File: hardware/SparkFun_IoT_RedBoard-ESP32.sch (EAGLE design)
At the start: 115 parts, among them J1 5.5x2.1mm Barrel, J13 QWIIC_RIGHT_ANGLE, J15 MICRO-SD-PUSH-PUSH-EXT-PIN, J2 USB C, J3 USB_SOLDER_PADS, J5 M10NO_SILK, Q1 MBT3904DW1T1, Q11 20V/4.2A/52mΩ/1.4W, Q13 20V/4.2A/52mΩ/1.4W, Q3 20V/4.2A/52mΩ/1.4W, Q5 20V/4.2A/52mΩ/1.4W, Q7 20V/4.2A/52mΩ/1.4W, Q9 20V/4.2A/52mΩ/1.4W, U1 ESP-WROOM-3232D-NARROW, U2 CH340C, U3 LM1117, U4 3.3V, U5 MCP73831, U6 MAX17048

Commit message: Design review updates
Rename files to remove "v01"
Update libraries
Adjust traces under SD card for keepout region
Change ESP32 footprint from narrow to standard
Change USB-C connector to 4-layer version
Add USB shield jumper
Move CC resistor positions
Adjust parts to be on grid where possible
Move Qwiic logo to top silk (also adjust Reset silk to avoid confusion)
Adjust layer numbers in copper to not overlap
Remove C14
Increase current rating of D1
Add silk to addressable LED
Remove extraneous mill lines
Remove Made in USA silk
Replace MEAS header and jumper with combo jumper
Add fuse value to schematic
Remove voltage ratings from capacitors in schematic
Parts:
- removed C14: 10uF, SparkFun-Capacitors:10UF-0603-6.3V-20%
- removed J14: (no value), SparkFun-Connectors:CONN_021X02_NO_SILK
- added JP15: SHLD, SparkFun-Jumpers:JUMPER-SMT_2_NC_TRACE_SILK
- D1: value 1A/40V/500mV -> 3A/40V/500mV; device SparkFun-DiscreteSemi:DIODE-SCHOTTKY-SS14 -> SparkFun-DiscreteSemi:DIODE-SCHOTTKY-B340A
- F1: value 6V/0.75A -> 6V/0.75A/1.5A
- J2: value USB C -> USB-C; device SparkFun-Connectors:USB_C_2-LAYER_PADS -> SparkFun-Connectors:USB_C_4-LAYER-ISOLATED
- JP10: value JUMPER-SMT_2_NC_TRACE_SILK -> JUMPER-COMBO_2_NC_TRACE; device SparkFun-Jumpers:JUMPER-SMT_2_NC_TRACE_SILK -> SparkFun-Jumpers:JUMPER-COMBO_2_NC_TRACE
- U1: value ESP-WROOM-3232D-NARROW -> ESP-WROOM-3232D; device SparkFun-RF:ESP-WROOM-3232D-NARROW -> SparkFun-RF:ESP-WROOM-3232D
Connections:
- new net SHLD: J2.SHLD, JP15.2
- net !DTR!: now also Q1G1.E; no longer Q1Q1.E
- net !RTS!: now also Q1G2.E; no longer Q1Q2.E
- net 3.3V: no longer C14.1
- net 5V_CHG: now also Q10G2.E, Q12G2.E; no longer Q10G$2.E, Q12G$2.E
- net 5V_EXT: now also Q12G1.E, Q6G1.E; no longer Q12G$1.E, Q6G$1.E
- net 5V_MEAS: now also Q4G2.E, Q6G2.E, Q8G2.E; no longer J14.2, Q4G$2.E, Q6G$2.E, Q8G$2.E
- net ESP32_0: now also Q1G1.C; no longer Q1Q1.C
- net ESP32_EN: now also Q1G2.C; no longer Q1Q2.C
- net GND: now also JP15.1, Q2G1.E, Q2G2.E; no longer C14.2, Q2Q1.E, Q2Q2.E
- net N$10: now also Q6G2.C; no longer Q6G$2.C
- net N$11: now also Q2G1.C; no longer Q2Q1.C
- net N$12: now also Q4G1.B, Q4G1.C, Q4G2.B; no longer Q4G$1.B, Q4G$1.C, Q4G$2.B
- net N$13: now also Q8G1.B, Q8G1.C, Q8G2.B; no longer Q8G$1.B, Q8G$1.C, Q8G$2.B
- net N$16: now also Q4G2.C; no longer Q4G$2.C
- net N$17: now also Q8G2.C; no longer Q8G$2.C
- net N$19: no longer J14.1
- net N$21: now also Q2G2.B; no longer Q2Q2.B
- net N$22: now also Q2G1.B, Q2G2.C; no longer Q2Q1.B, Q2Q2.C
- net N$23: now also Q10G2.C; no longer Q10G$2.C
- net N$24: now also Q1G1.B; no longer Q1Q1.B
- net N$25: now also Q1G2.B; no longer Q1Q2.B
- net N$26: now also Q10G1.B, Q10G1.C, Q10G2.B; no longer Q10G$1.B, Q10G$1.C, Q10G$2.B
- net N$28: now also Q12G2.C; no longer Q12G$2.C
- net N$29: now also Q12G1.B, Q12G1.C, Q12G2.B; no longer Q12G$1.B, Q12G$1.C, Q12G$2.B
- net N$8: now also Q6G1.B, Q6G1.C, Q6G2.B; no longer Q6G$1.B, Q6G$1.C, Q6G$2.B
- net VUSB_PROT: now also Q4G1.E; no longer Q4G$1.E
- net V_BATT: now also Q8G1.E; no longer Q8G$1.E
- net V_USB: now also Q10G1.E; no longer Q10G$1.E
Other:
- note added: "Open jumper to measure board current on J10"
- note removed: "16V"
- note removed: "25V"
- note removed: "35V"
- note removed: "Open jumper to measure board current on J14"
- moved on the sheet: C12, C13, J2, J3, U4

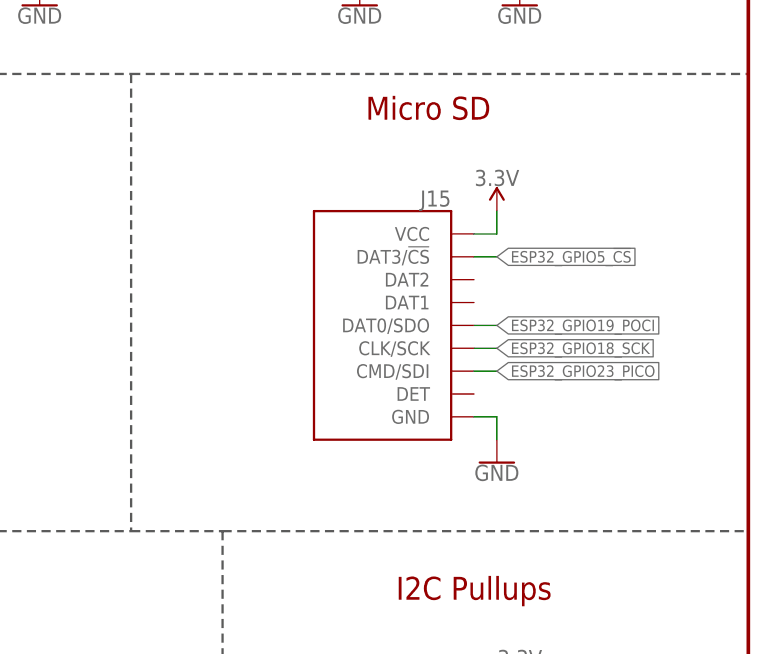
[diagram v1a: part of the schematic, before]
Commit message: More design review updates
Add center positive silk marker to barrel jack
Fix air wire errors in ULP by connecting with traces
Add SD card detection with NO jumper to GPIO16
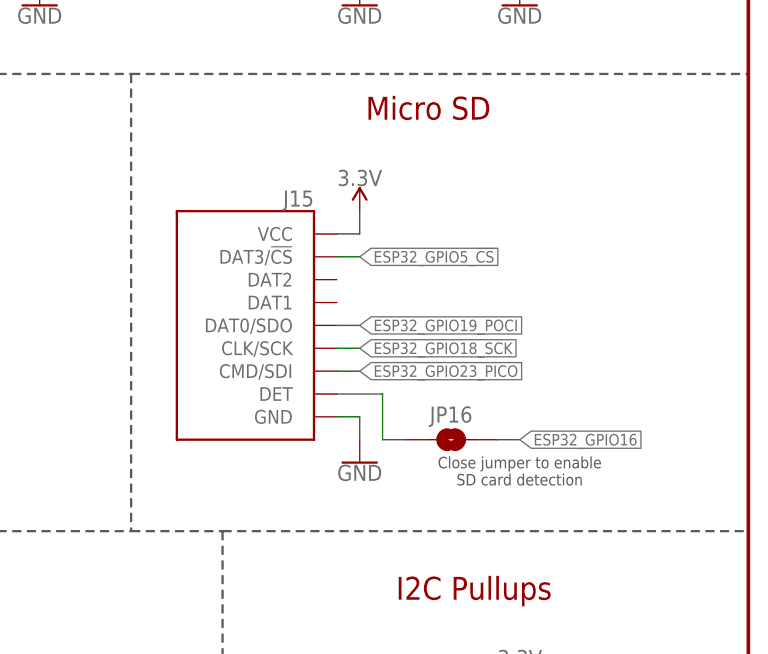
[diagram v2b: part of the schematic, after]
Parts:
- added JP16: SD_DET, SparkFun-Jumpers:JUMPER-SMT_2_NO_SILK
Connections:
- new net N$27: J15.DET, JP16.1
- net ESP32_GPIO16: now also JP16.2
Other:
- note added: "Close jumper to enable SD card detection"
- moved on the sheet: J15
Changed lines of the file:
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@@
 <part name="GND56" library="SparkFun-PowerSymbols" deviceset="GND" device=""/>
 <part name="F1" library="SparkFun-Fuses" deviceset="PPTC" device="_0.75A" value="6V/0.75A/1.5A"/>
+<part name="JP16" library="SparkFun-Jumpers" deviceset="JUMPER-SMT_2_NO" device="_SILK" package3d_urn="urn:adsk.eagle:package:39279/1" value="SD_DET"/>
 </parts>
 <sheets>
@@
 <wire x1="317.5" y1="203.2" x2="317.5" y2="236.22" width="0.254" layer="97" style="longdash"/>
 <text x="330.2" y="228.6" size="2.54" layer="94" font="vector" ratio="11" align="bottom-center">RGB LED</text>
+<text x="406.4" y="93.98" size="1.27" layer="97" font="vector" align="bottom-center">Close jumper to enable
+SD card detection</text>
 </plain>
 <instances>
@@
 <attribute name="VALUE" x="50.8" y="152.908" size="1.778" layer="96" font="vector" rot="R180" align="center" display="off"/>
 </instance>
-<instance part="J15" gate="J1" x="393.7" y="111.76" smashed="yes" rot="MR0">
-<attribute name="NAME" x="398.78" y="124.968" size="1.778" layer="95" rot="MR0"/>
-<attribute name="VALUE" x="398.78" y="96.52" size="1.778" layer="96" rot="MR0" display="off"/>
-</instance>
-<instance part="SUPPLY27" gate="G$1" x="403.86" y="124.46" smashed="yes">
-<attribute name="VALUE" x="403.86" y="127.254" size="1.778" layer="96" align="bottom-center"/>
-</instance>
-<instance part="GND33" gate="1" x="403.86" y="96.52" smashed="yes">
-<attribute name="VALUE" x="403.86" y="96.266" size="1.778" layer="96" align="top-center"/>
+<instance part="J15" gate="J1" x="378.46" y="111.76" smashed="yes" rot="MR0">
+<attribute name="NAME" x="383.54" y="124.968" size="1.778" layer="95" rot="MR0"/>
+<attribute name="VALUE" x="383.54" y="96.52" size="1.778" layer="96" rot="MR0" display="off"/>
+</instance>
+<instance part="SUPPLY27" gate="G$1" x="388.62" y="124.46" smashed="yes">
+<attribute name="VALUE" x="388.62" y="127.254" size="1.778" layer="96" align="bottom-center"/>
+</instance>
+<instance part="GND33" gate="1" x="388.62" y="96.52" smashed="yes">
+<attribute name="VALUE" x="388.62" y="96.266" size="1.778" layer="96" align="top-center"/>
 </instance>
 <instance part="GND24" gate="1" x="144.78" y="5.08" smashed="yes">
@@
 <attribute name="NAME" x="159.893" y="15.113" size="1.778" layer="95" font="vector" align="bottom-center"/>
 <attribute name="VALUE" x="161.29" y="9.906" size="1.778" layer="96" font="vector" align="top-center"/>
+</instance>
+<instance part="JP16" gate="G$1" x="398.78" y="99.06" smashed="yes">
+<attribute name="NAME" x="398.78" y="101.854" size="1.778" layer="95" font="vector" align="center"/>
 </instance>
 </instances>
@@
 <pinref part="J15" gate="J1" pin="GND"/>
 <pinref part="GND33" gate="1" pin="GND"/>
-<wire x1="401.32" y1="101.6" x2="403.86" y2="101.6" width="0.1524" layer="91"/>
-<wire x1="403.86" y1="101.6" x2="403.86" y2="99.06" width="0.1524" layer="91"/>
+<wire x1="386.08" y1="101.6" x2="388.62" y2="101.6" width="0.1524" layer="91"/>
+<wire x1="388.62" y1="101.6" x2="388.62" y2="99.06" width="0.1524" layer="91"/>
 </segment>
 <segment>
@@
 <segment>
 <pinref part="SUPPLY27" gate="G$1" pin="3.3V"/>
-<wire x1="403.86" y1="124.46" x2="403.86" y2="121.92" width="0.1524" layer="91"/>
+<wire x1="388.62" y1="124.46" x2="388.62" y2="121.92" width="0.1524" layer="91"/>
 <pinref part="J15" gate="J1" pin="VCC"/>
-<wire x1="403.86" y1="121.92" x2="401.32" y2="121.92" width="0.1524" layer="91"/>
+<wire x1="388.62" y1="121.92" x2="386.08" y2="121.92" width="0.1524" layer="91"/>
 </segment>
 <segment>
@@
 <segment>
 <pinref part="J15" gate="J1" pin="DAT3/!CS!"/>
-<wire x1="401.32" y1="119.38" x2="403.86" y2="119.38" width="0.1524" layer="91"/>
-<label x="403.86" y="119.38" size="1.27" layer="95" xref="yes"/>
+<wire x1="386.08" y1="119.38" x2="388.62" y2="119.38" width="0.1524" layer="91"/>
+<label x="388.62" y="119.38" size="1.27" layer="95" xref="yes"/>
 </segment>
 <segment>
@@
 <segment>
 <pinref part="J15" gate="J1" pin="CLK/SCK"/>
-<wire x1="401.32" y1="109.22" x2="403.86" y2="109.22" width="0.1524" layer="91"/>
-<label x="403.86" y="109.22" size="1.27" layer="95" xref="yes"/>
+<wire x1="386.08" y1="109.22" x2="388.62" y2="109.22" width="0.1524" layer="91"/>
+<label x="388.62" y="109.22" size="1.27" layer="95" xref="yes"/>
 </segment>
 <segment>
@@
 <segment>
 <pinref part="J15" gate="J1" pin="DAT0/SDO"/>
-<wire x1="401.32" y1="111.76" x2="403.86" y2="111.76" width="0.1524" layer="91"/>
-<label x="403.86" y="111.76" size="1.27" layer="95" xref="yes"/>
+<wire x1="386.08" y1="111.76" x2="388.62" y2="111.76" width="0.1524" layer="91"/>
+<label x="388.62" y="111.76" size="1.27" layer="95" xref="yes"/>
 </segment>
 <segment>
@@
 <label x="177.8" y="213.36" size="1.27" layer="95" rot="R180" xref="yes"/>
 <pinref part="J8" gate="G$1" pin="6"/>
+</segment>
+<segment>
+<pinref part="JP16" gate="G$1" pin="2"/>
+<wire x1="403.86" y1="99.06" x2="406.4" y2="99.06" width="0.1524" layer="91"/>
+<label x="406.4" y="99.06" size="1.27" layer="95" xref="yes"/>
 </segment>
 </net>
@@
 <segment>
 <pinref part="J15" gate="J1" pin="CMD/SDI"/>
-<wire x1="401.32" y1="106.68" x2="403.86" y2="106.68" width="0.1524" layer="91"/>
-<label x="403.86" y="106.68" size="1.27" layer="95" xref="yes"/>
+<wire x1="386.08" y1="106.68" x2="388.62" y2="106.68" width="0.1524" layer="91"/>
+<label x="388.62" y="106.68" size="1.27" layer="95" xref="yes"/>
 </segment>
 <segment>
@@
 </segment>
 </net>
+<net name="N$27" class="0">
+<segment>
+<pinref part="J15" gate="J1" pin="DET"/>
+<wire x1="386.08" y1="104.14" x2="391.16" y2="104.14" width="0.1524" layer="91"/>
+<wire x1="391.16" y1="104.14" x2="391.16" y2="99.06" width="0.1524" layer="91"/>
+<pinref part="JP16" gate="G$1" pin="1"/>
+<wire x1="391.16" y1="99.06" x2="393.7" y2="99.06" width="0.1524" layer="91"/>
+</segment>
+</net>

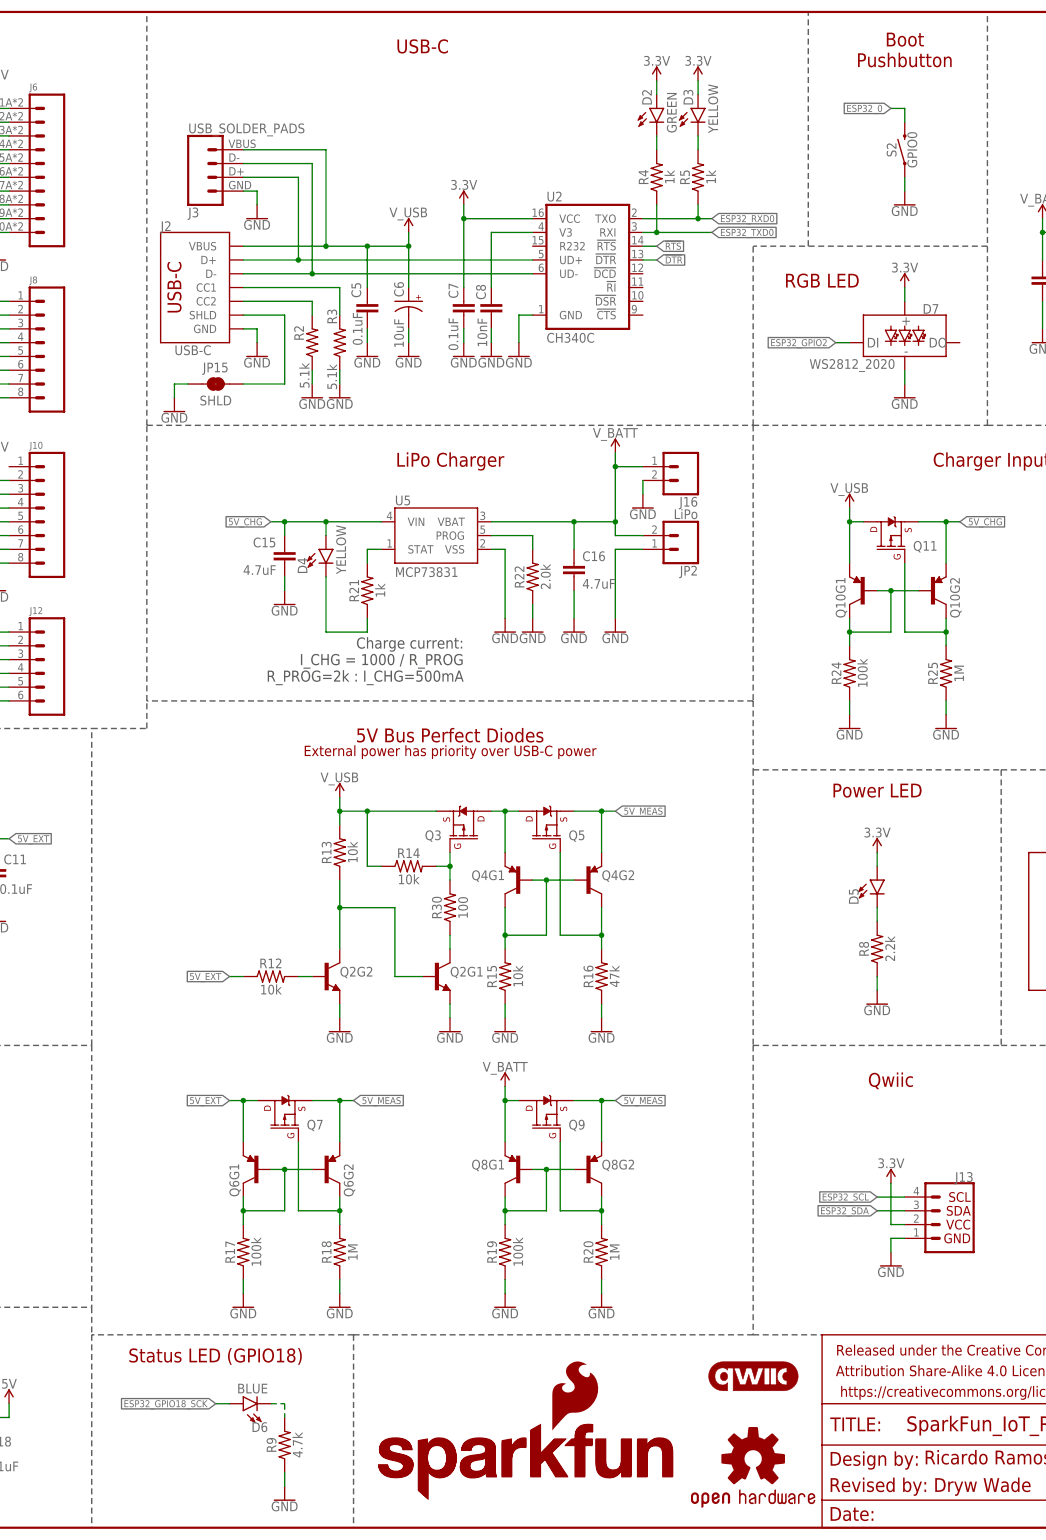
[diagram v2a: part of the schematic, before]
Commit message: Add NC jumper for each LED
Also fix barrel jack voltage silk
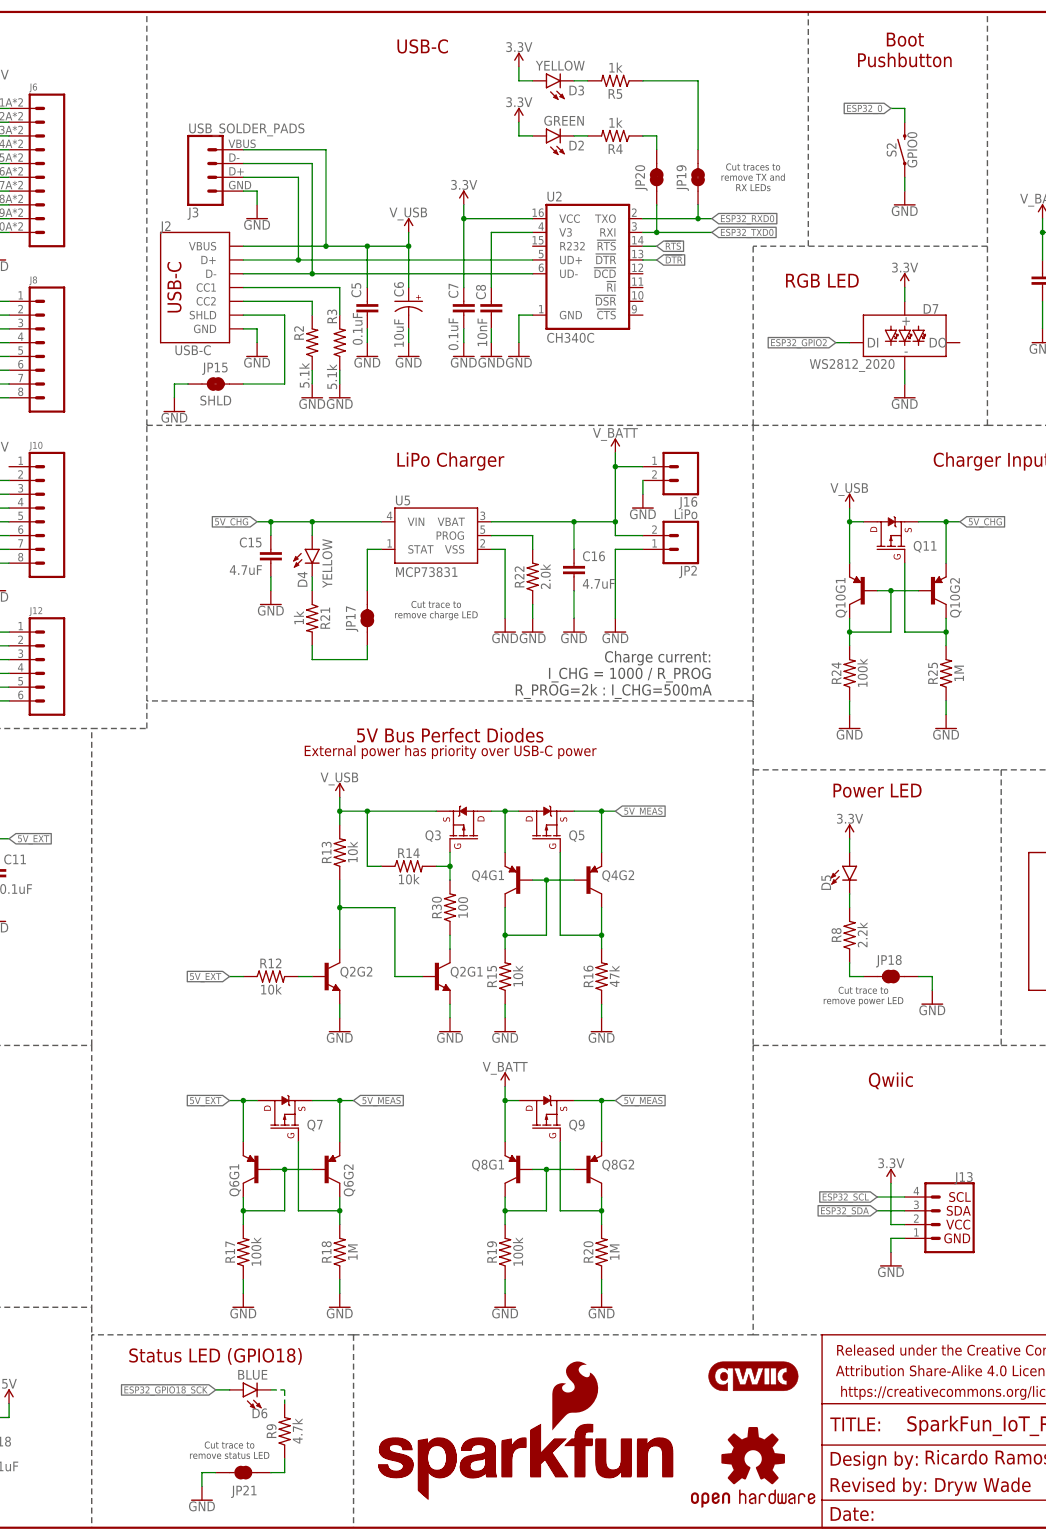
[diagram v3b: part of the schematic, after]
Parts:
- added JP17, JP18, JP19, JP20, JP21: JUMPER-SMT_2_NC_TRACE_SILK, SparkFun-Jumpers:JUMPER-SMT_2_NC_TRACE_SILK
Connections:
- new net N$30: JP20.2, R4.1
- new net N$31: JP19.2, R5.1
- new net N$33: JP18.2, R8.1
- new net N$34: JP21.2, R9.1
- new net N$4: JP17.1, R21.2
- net ESP32_RXD0: now also JP19.1; no longer R5.1
- net ESP32_TXD0: now also JP20.1; no longer R4.1
- net GND: now also JP18.1, JP21.1; no longer R8.1, R9.1
- net N$1: now also JP17.2; no longer R21.2
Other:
- note added: "Cut trace to remove charge LED"
- note added: "Cut trace to remove power LED"
- note added: "Cut trace to remove status LED"
- note added: "Cut traces to remove TX and RX LEDs"
- moved on the sheet: C15, D2, D3, D4, D5, D6, R21, R4, R5, R8, R9

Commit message: Update version number to v10
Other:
- note added: "v10"
- note removed: "v02"
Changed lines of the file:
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@@
 T.Igoe, G.Martino, D.Mellis</text>
 <text x="348.996" y="11.684" size="2.54" layer="94" font="vector">Ricardo Ramos</text>
-<text x="421.64" y="7.62" size="2.54" layer="94" font="vector">v02</text>
+<text x="421.64" y="7.62" size="2.54" layer="94" font="vector">v10</text>
 <text x="144.78" y="25.4" size="1.27" layer="97" font="vector">This is the penny-in-the-fuse
 jumper. Close only if you know
